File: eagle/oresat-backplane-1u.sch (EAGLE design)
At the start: 36 parts, among them J1 5-104196-5, J3 HARWIN-M50-3002045

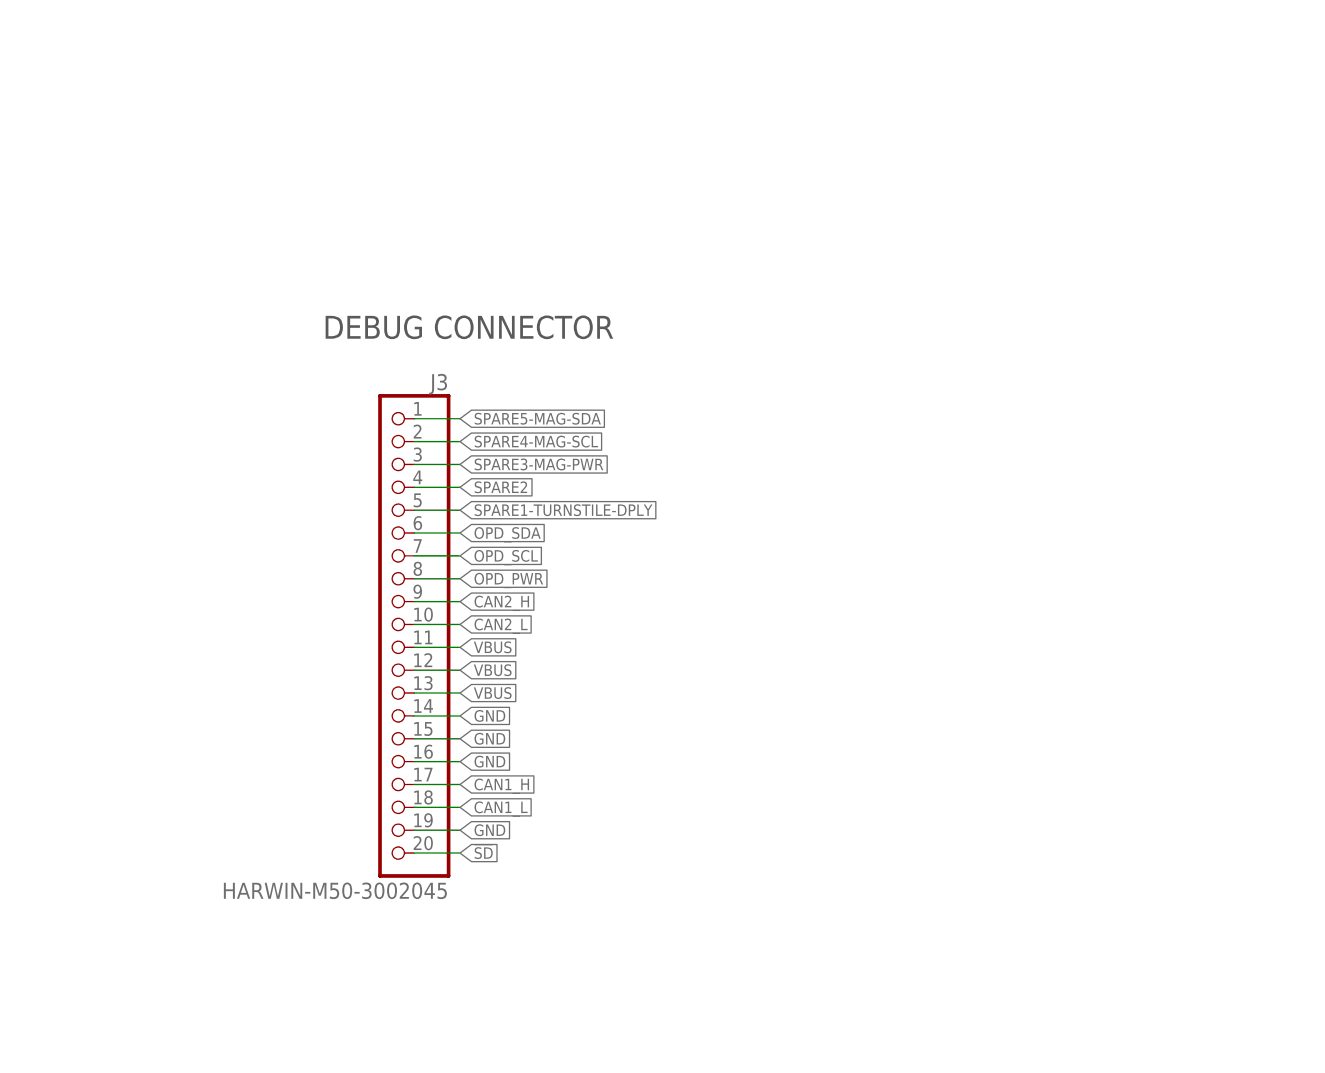
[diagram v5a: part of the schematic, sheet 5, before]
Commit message: Updated with corrected debug connector. Footprint didn't change, so no change to version.
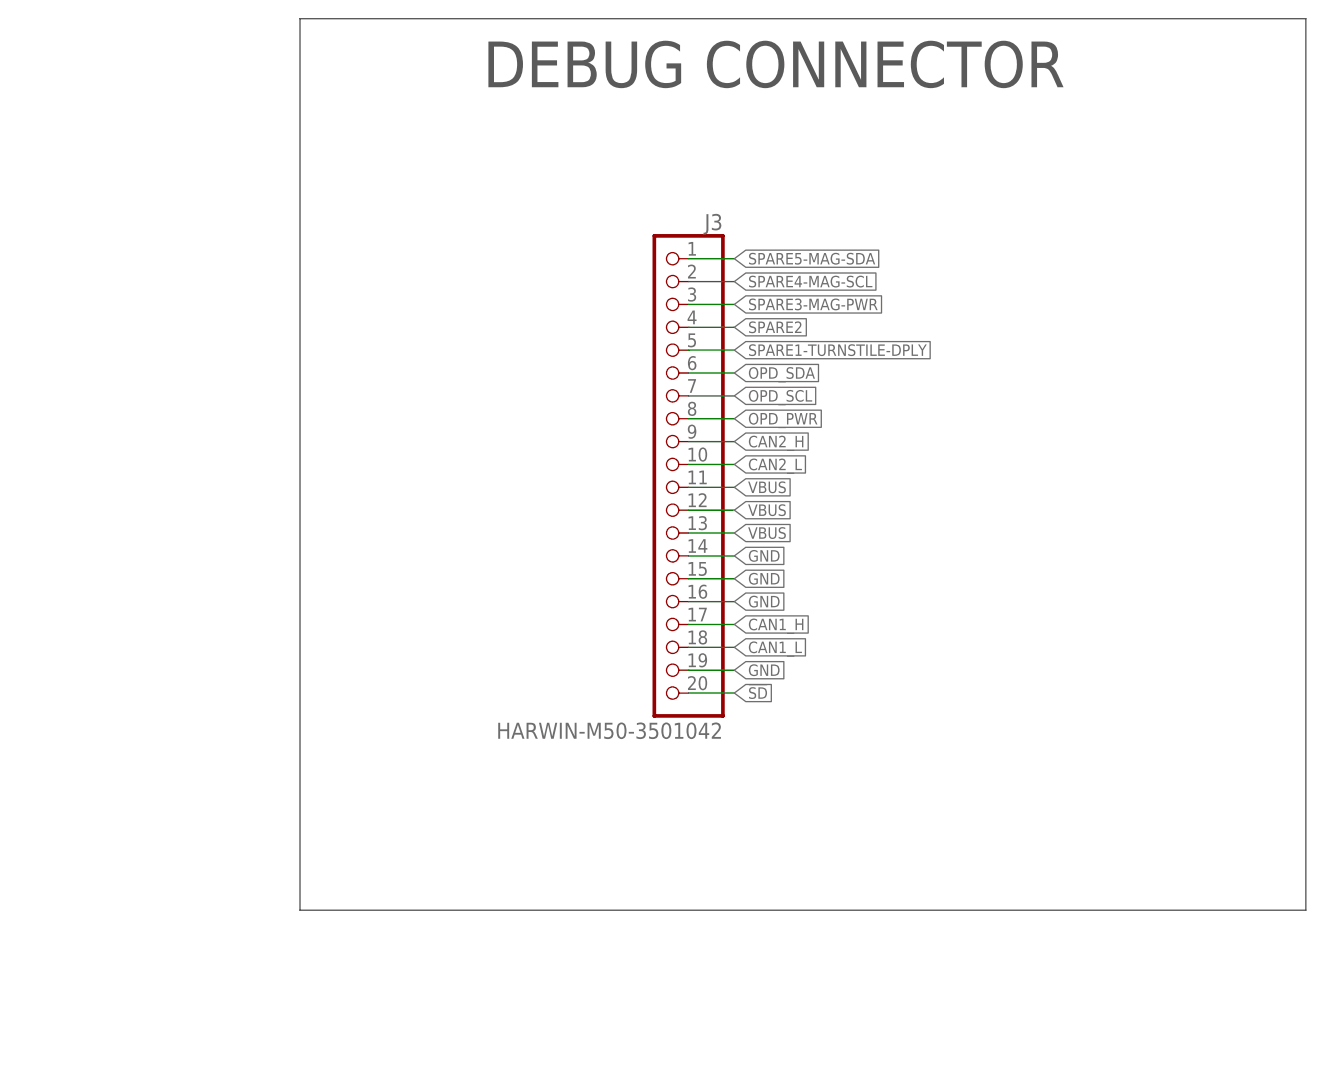
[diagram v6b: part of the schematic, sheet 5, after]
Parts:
- J3: value HARWIN-M50-3002045 -> HARWIN-M50-3501042; device J-Harwin-M50-3002045-20pin-1.27-F-and-M-vertical-th:HARWIN-M50-3002045 -> J-Harwin-M50-3501042-20pin-M-1.27mm-vertical-th:HARWIN-M50-3501042
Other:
- moved on the sheet: J3
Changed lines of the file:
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@@
 <part name="J1" library="J-TE-5-104196-5-RA-1.27mm-female-th" deviceset="5-104196-5" device=""/>
 <part name="GND6" library="supply" deviceset="GND" device=""/>
-<part name="J3" library="J-Harwin-M50-3002045-20pin-1.27-F-and-M-vertical-th" deviceset="HARWIN-M50-3002045" device=""/>
+<part name="J3" library="J-Harwin-M50-3501042-20pin-M-1.27mm-vertical-th" deviceset="HARWIN-M50-3501042" device=""/>
 <part name="GND7" library="supply" deviceset="GND" device=""/>
 <part name="U$1" library="oresat-flight-marker" deviceset="FLIGHMARKER" device="NEW"/>
@@
 <description>Slot 5</description>
 <plain>
-<text x="104.14" y="127" size="2.54" layer="97">DEBUG CONNECTOR</text>
+<text x="121.92" y="154.94" size="5.08" layer="97">DEBUG CONNECTOR</text>
+<wire x1="101.6" y1="162.56" x2="213.36" y2="162.56" width="0.1524" layer="97"/>
+<wire x1="213.36" y1="162.56" x2="213.36" y2="63.5" width="0.1524" layer="97"/>
+<wire x1="213.36" y1="63.5" x2="101.6" y2="63.5" width="0.1524" layer="97"/>
+<wire x1="101.6" y1="63.5" x2="101.6" y2="162.56" width="0.1524" layer="97"/>
 </plain>
 <instances>
@@
 <attribute name="NAME" x="12.7" y="127" size="1.27" layer="95"/>
 </instance>
-<instance part="J3" gate="G$1" x="111.76" y="95.25" smashed="yes" rot="MR0">
-<attribute name="NAME" x="118.11" y="121.285" size="1.778" layer="95" rot="MR0"/>
-<attribute name="VALUE" x="118.11" y="64.77" size="1.778" layer="96" rot="MR0"/>
+<instance part="J3" gate="G$1" x="142.24" y="113.03" smashed="yes" rot="MR0">
+<attribute name="NAME" x="148.59" y="139.065" size="1.778" layer="95" rot="MR0"/>
+<attribute name="VALUE" x="148.59" y="82.55" size="1.778" layer="96" rot="MR0"/>
 </instance>
 </instances>
@@
 </segment>
 <segment>
-<wire x1="119.38" y1="85.09" x2="114.3" y2="85.09" width="0.1524" layer="91"/>
-<label x="119.38" y="85.09" size="1.27" layer="95" xref="yes"/>
+<wire x1="149.86" y1="102.87" x2="144.78" y2="102.87" width="0.1524" layer="91"/>
+<label x="149.86" y="102.87" size="1.27" layer="95" xref="yes"/>
 <pinref part="J3" gate="G$1" pin="14"/>
 </segment>
 <segment>
-<wire x1="119.38" y1="82.55" x2="114.3" y2="82.55" width="0.1524" layer="91"/>
-<label x="119.38" y="82.55" size="1.27" layer="95" xref="yes"/>
+<wire x1="149.86" y1="100.33" x2="144.78" y2="100.33" width="0.1524" layer="91"/>
+<label x="149.86" y="100.33" size="1.27" layer="95" xref="yes"/>
 <pinref part="J3" gate="G$1" pin="15"/>
 </segment>
 <segment>
-<wire x1="119.38" y1="72.39" x2="114.3" y2="72.39" width="0.1524" layer="91"/>
-<label x="119.38" y="72.39" size="1.27" layer="95" xref="yes"/>
+<wire x1="149.86" y1="90.17" x2="144.78" y2="90.17" width="0.1524" layer="91"/>
+<label x="149.86" y="90.17" size="1.27" layer="95" xref="yes"/>
 <pinref part="J3" gate="G$1" pin="19"/>
 </segment>
 <segment>
-<wire x1="119.38" y1="80.01" x2="114.3" y2="80.01" width="0.1524" layer="91"/>
-<label x="119.38" y="80.01" size="1.27" layer="95" xref="yes"/>
+<wire x1="149.86" y1="97.79" x2="144.78" y2="97.79" width="0.1524" layer="91"/>
+<label x="149.86" y="97.79" size="1.27" layer="95" xref="yes"/>
 <pinref part="J3" gate="G$1" pin="16"/>
 </segment>
@@
 </segment>
 <segment>
-<wire x1="114.3" y1="118.11" x2="119.38" y2="118.11" width="0.1524" layer="91"/>
-<label x="119.38" y="118.11" size="1.27" layer="95" xref="yes"/>
+<wire x1="144.78" y1="135.89" x2="149.86" y2="135.89" width="0.1524" layer="91"/>
+<label x="149.86" y="135.89" size="1.27" layer="95" xref="yes"/>
 <pinref part="J3" gate="G$1" pin="1"/>
 </segment>
@@
 </segment>
 <segment>
-<wire x1="114.3" y1="115.57" x2="119.38" y2="115.57" width="0.1524" layer="91"/>
-<label x="119.38" y="115.57" size="1.27" layer="95" xref="yes"/>
+<wire x1="144.78" y1="133.35" x2="149.86" y2="133.35" width="0.1524" layer="91"/>
+<label x="149.86" y="133.35" size="1.27" layer="95" xref="yes"/>
 <pinref part="J3" gate="G$1" pin="2"/>
 </segment>
@@
 </segment>
 <segment>
-<wire x1="114.3" y1="113.03" x2="119.38" y2="113.03" width="0.1524" layer="91"/>
-<label x="119.38" y="113.03" size="1.27" layer="95" xref="yes"/>
+<wire x1="144.78" y1="130.81" x2="149.86" y2="130.81" width="0.1524" layer="91"/>
+<label x="149.86" y="130.81" size="1.27" layer="95" xref="yes"/>
 <pinref part="J3" gate="G$1" pin="3"/>
 </segment>
@@
 </segment>
 <segment>
-<wire x1="119.38" y1="110.49" x2="114.3" y2="110.49" width="0.1524" layer="91"/>
-<label x="119.38" y="110.49" size="1.27" layer="95" xref="yes"/>
+<wire x1="149.86" y1="128.27" x2="144.78" y2="128.27" width="0.1524" layer="91"/>
+<label x="149.86" y="128.27" size="1.27" layer="95" xref="yes"/>
 <pinref part="J3" gate="G$1" pin="4"/>
 </segment>
@@
 </segment>
 <segment>
-<wire x1="119.38" y1="107.95" x2="114.3" y2="107.95" width="0.1524" layer="91"/>
-<label x="119.38" y="107.95" size="1.27" layer="95" xref="yes"/>
+<wire x1="149.86" y1="125.73" x2="144.78" y2="125.73" width="0.1524" layer="91"/>
+<label x="149.86" y="125.73" size="1.27" layer="95" xref="yes"/>
 <pinref part="J3" gate="G$1" pin="5"/>
 </segment>
@@
 </segment>
 <segment>
-<wire x1="119.38" y1="105.41" x2="114.3" y2="105.41" width="0.1524" layer="91"/>
-<label x="119.38" y="105.41" size="1.27" layer="95" xref="yes"/>
+<wire x1="149.86" y1="123.19" x2="144.78" y2="123.19" width="0.1524" layer="91"/>
+<label x="149.86" y="123.19" size="1.27" layer="95" xref="yes"/>
 <pinref part="J3" gate="G$1" pin="6"/>
 </segment>
@@
 </segment>
 <segment>
-<wire x1="119.38" y1="102.87" x2="114.3" y2="102.87" width="0.1524" layer="91"/>
-<label x="119.38" y="102.87" size="1.27" layer="95" xref="yes"/>
+<wire x1="149.86" y1="120.65" x2="144.78" y2="120.65" width="0.1524" layer="91"/>
+<label x="149.86" y="120.65" size="1.27" layer="95" xref="yes"/>
 <pinref part="J3" gate="G$1" pin="7"/>
 </segment>
@@
 </segment>
 <segment>
-<wire x1="119.38" y1="100.33" x2="114.3" y2="100.33" width="0.1524" layer="91"/>
-<label x="119.38" y="100.33" size="1.27" layer="95" xref="yes"/>
+<wire x1="149.86" y1="118.11" x2="144.78" y2="118.11" width="0.1524" layer="91"/>
+<label x="149.86" y="118.11" size="1.27" layer="95" xref="yes"/>
 <pinref part="J3" gate="G$1" pin="8"/>
 </segment>
@@
 </segment>
 <segment>
-<wire x1="114.3" y1="97.79" x2="119.38" y2="97.79" width="0.1524" layer="91"/>
-<label x="119.38" y="97.79" size="1.27" layer="95" xref="yes"/>
+<wire x1="144.78" y1="115.57" x2="149.86" y2="115.57" width="0.1524" layer="91"/>
+<label x="149.86" y="115.57" size="1.27" layer="95" xref="yes"/>
 <pinref part="J3" gate="G$1" pin="9"/>
 </segment>
@@
 </segment>
 <segment>
-<wire x1="119.38" y1="95.25" x2="114.3" y2="95.25" width="0.1524" layer="91"/>
-<label x="119.38" y="95.25" size="1.27" layer="95" xref="yes"/>
+<wire x1="149.86" y1="113.03" x2="144.78" y2="113.03" width="0.1524" layer="91"/>
+<label x="149.86" y="113.03" size="1.27" layer="95" xref="yes"/>
 <pinref part="J3" gate="G$1" pin="10"/>
 </segment>
@@
 </segment>
 <segment>
-<wire x1="119.38" y1="92.71" x2="114.3" y2="92.71" width="0.1524" layer="91"/>
-<label x="119.38" y="92.71" size="1.27" layer="95" xref="yes"/>
+<wire x1="149.86" y1="110.49" x2="144.78" y2="110.49" width="0.1524" layer="91"/>
+<label x="149.86" y="110.49" size="1.27" layer="95" xref="yes"/>
 <pinref part="J3" gate="G$1" pin="11"/>
 </segment>
 <segment>
-<wire x1="119.38" y1="90.17" x2="114.3" y2="90.17" width="0.1524" layer="91"/>
-<label x="119.38" y="90.17" size="1.27" layer="95" xref="yes"/>
+<wire x1="149.86" y1="107.95" x2="144.78" y2="107.95" width="0.1524" layer="91"/>
+<label x="149.86" y="107.95" size="1.27" layer="95" xref="yes"/>
 <pinref part="J3" gate="G$1" pin="12"/>
 </segment>
 <segment>
-<wire x1="119.38" y1="87.63" x2="114.3" y2="87.63" width="0.1524" layer="91"/>
-<label x="119.38" y="87.63" size="1.27" layer="95" xref="yes"/>
+<wire x1="149.86" y1="105.41" x2="144.78" y2="105.41" width="0.1524" layer="91"/>
+<label x="149.86" y="105.41" size="1.27" layer="95" xref="yes"/>
 <pinref part="J3" gate="G$1" pin="13"/>
 </segment>
@@
 </segment>
 <segment>
-<wire x1="119.38" y1="77.47" x2="114.3" y2="77.47" width="0.1524" layer="91"/>
-<label x="119.38" y="77.47" size="1.27" layer="95" xref="yes"/>
+<wire x1="149.86" y1="95.25" x2="144.78" y2="95.25" width="0.1524" layer="91"/>
+<label x="149.86" y="95.25" size="1.27" layer="95" xref="yes"/>
 <pinref part="J3" gate="G$1" pin="17"/>
 </segment>
@@
 </segment>
 <segment>
-<wire x1="119.38" y1="74.93" x2="114.3" y2="74.93" width="0.1524" layer="91"/>
-<label x="119.38" y="74.93" size="1.27" layer="95" xref="yes"/>
+<wire x1="149.86" y1="92.71" x2="144.78" y2="92.71" width="0.1524" layer="91"/>
+<label x="149.86" y="92.71" size="1.27" layer="95" xref="yes"/>
 <pinref part="J3" gate="G$1" pin="18"/>
 </segment>
@@
 </segment>
 <segment>
-<wire x1="119.38" y1="69.85" x2="114.3" y2="69.85" width="0.1524" layer="91"/>
-<label x="119.38" y="69.85" size="1.27" layer="95" xref="yes"/>
+<wire x1="149.86" y1="87.63" x2="144.78" y2="87.63" width="0.1524" layer="91"/>
+<label x="149.86" y="87.63" size="1.27" layer="95" xref="yes"/>
 <pinref part="J3" gate="G$1" pin="20"/>
 </segment>

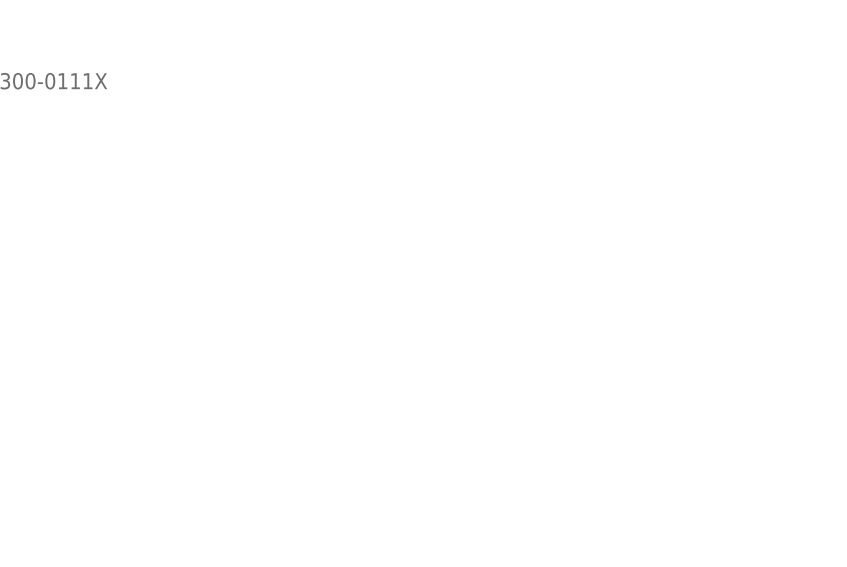
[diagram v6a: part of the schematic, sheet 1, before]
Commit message: Version 1.3. No significant difference with v1.2 besides added TPLACE block, updated not for flight marker, and fiducials just in case.
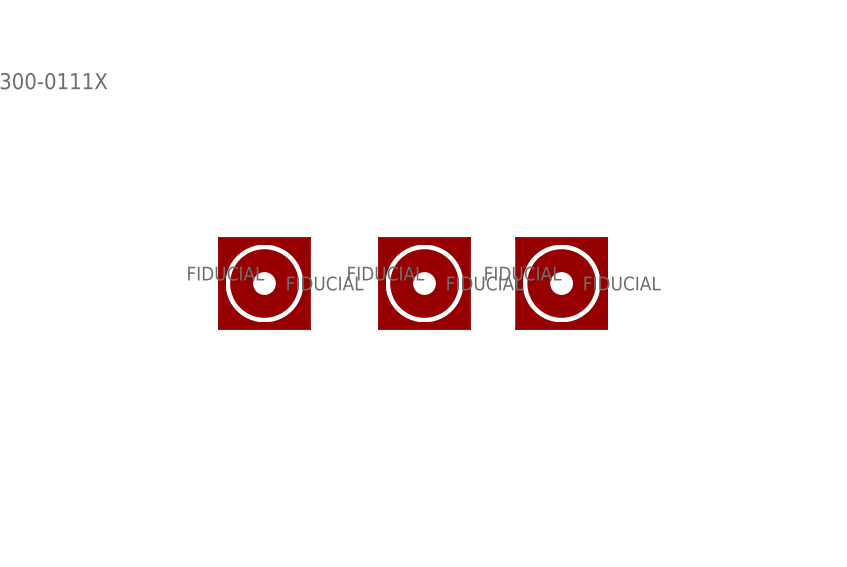
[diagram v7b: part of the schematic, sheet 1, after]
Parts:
- added FIDUCIAL1, FIDUCIAL2, FIDUCIAL3: FIDUCIAL-1.0X2.0, dock_v2:FIDUCIAL-1.0X2.0
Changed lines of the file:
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@@
 <layer number="99" name="SpiceOrder" color="7" fill="1" visible="yes" active="yes"/>
 <layer number="100" name="DXF" color="61" fill="1" visible="yes" active="yes"/>
+<layer number="101" name="Hidden" color="7" fill="1" visible="yes" active="yes"/>
+<layer number="102" name="Changes" color="7" fill="1" visible="yes" active="yes"/>
+<layer number="103" name="tMap" color="7" fill="1" visible="yes" active="yes"/>
+<layer number="104" name="Name" color="7" fill="1" visible="yes" active="yes"/>
+<layer number="105" name="Beschreib" color="7" fill="1" visible="yes" active="yes"/>
+<layer number="106" name="BGA-Top" color="7" fill="1" visible="yes" active="yes"/>
+<layer number="107" name="BD-Top" color="7" fill="1" visible="yes" active="yes"/>
+<layer number="108" name="dxf_notes" color="7" fill="1" visible="yes" active="yes"/>
+<layer number="110" name="labels" color="7" fill="1" visible="yes" active="yes"/>
+<layer number="111" name="print" color="7" fill="1" visible="yes" active="yes"/>
+<layer number="112" name="hints" color="7" fill="1" visible="yes" active="yes"/>
+<layer number="116" name="Patch_BOT" color="7" fill="1" visible="yes" active="yes"/>
+<layer number="121" name="_tsilk" color="7" fill="1" visible="yes" active="yes"/>
+<layer number="122" name="_bsilk" color="7" fill="1" visible="yes" active="yes"/>
+<layer number="125" name="_tNames" color="7" fill="1" visible="yes" active="yes"/>
+<layer number="144" name="Drill_legend" color="7" fill="1" visible="yes" active="yes"/>
+<layer number="151" name="HeatSink" color="7" fill="1" visible="yes" active="yes"/>
+<layer number="200" name="200bmp" color="7" fill="1" visible="yes" active="yes"/>
+<layer number="201" name="201bmp" color="7" fill="1" visible="yes" active="yes"/>
+<layer number="202" name="202bmp" color="7" fill="1" visible="yes" active="yes"/>
+<layer number="203" name="203bmp" color="7" fill="1" visible="yes" active="yes"/>
+<layer number="204" name="204bmp" color="7" fill="1" visible="yes" active="yes"/>
+<layer number="205" name="205bmp" color="7" fill="1" visible="yes" active="yes"/>
+<layer number="206" name="206bmp" color="7" fill="1" visible="yes" active="yes"/>
+<layer number="207" name="207bmp" color="7" fill="1" visible="yes" active="yes"/>
+<layer number="208" name="208bmp" color="7" fill="1" visible="yes" active="yes"/>
+<layer number="209" name="209bmp" color="7" fill="1" visible="yes" active="yes"/>
+<layer number="210" name="210bmp" color="7" fill="1" visible="yes" active="yes"/>
+<layer number="211" name="211bmp" color="7" fill="1" visible="yes" active="yes"/>
+<layer number="212" name="212bmp" color="7" fill="1" visible="yes" active="yes"/>
+<layer number="213" name="213bmp" color="7" fill="1" visible="yes" active="yes"/>
+<layer number="214" name="214bmp" color="7" fill="1" visible="yes" active="yes"/>
+<layer number="215" name="215bmp" color="7" fill="1" visible="yes" active="yes"/>
+<layer number="216" name="216bmp" color="7" fill="1" visible="yes" active="yes"/>
 <layer number="217" name="217bmp" color="18" fill="1" visible="no" active="no"/>
 <layer number="218" name="218bmp" color="19" fill="1" visible="no" active="no"/>
@@
 <layer number="223" name="223bmp" color="24" fill="1" visible="no" active="no"/>
 <layer number="224" name="224bmp" color="25" fill="1" visible="no" active="no"/>
+<layer number="250" name="Descript" color="7" fill="1" visible="yes" active="yes"/>
+<layer number="251" name="SMDround" color="7" fill="1" visible="yes" active="yes"/>
+<layer number="254" name="cooling" color="7" fill="1" visible="yes" active="yes"/>
 </layers>
 <schematic xreflabel="%F%N/%S.%C%R" xrefpart="/%S.%C%R">
@@
 <part name="GND7" library="supply" deviceset="GND" device=""/>
 <part name="U$1" library="oresat-flight-marker" deviceset="FLIGHMARKER" device="NEW"/>
+<part name="FIDUCIAL1" library="dock_v2" deviceset="FIDUCIAL" device="-1.0X2.0"/>
+<part name="FIDUCIAL2" library="dock_v2" deviceset="FIDUCIAL" device="-1.0X2.0"/>
+<part name="FIDUCIAL3" library="dock_v2" deviceset="FIDUCIAL" device="-1.0X2.0"/>
 </parts>
 <sheets>
@@
 <instance part="GND3" gate="G1" x="147.32" y="68.58" smashed="yes"/>
 <instance part="U$1" gate="G$1" x="121.92" y="2.54" smashed="yes"/>
+<instance part="FIDUCIAL1" gate="FIDUCIAL" x="200.66" y="45.72" smashed="yes"/>
+<instance part="FIDUCIAL2" gate="FIDUCIAL" x="218.44" y="45.72" smashed="yes"/>
+<instance part="FIDUCIAL3" gate="FIDUCIAL" x="233.68" y="45.72" smashed="yes"/>
 </instances>
 <busses>
